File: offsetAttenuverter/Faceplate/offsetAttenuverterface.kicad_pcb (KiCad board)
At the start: 2 copper layers, 20.3 x 128.6 mm, 10 parts

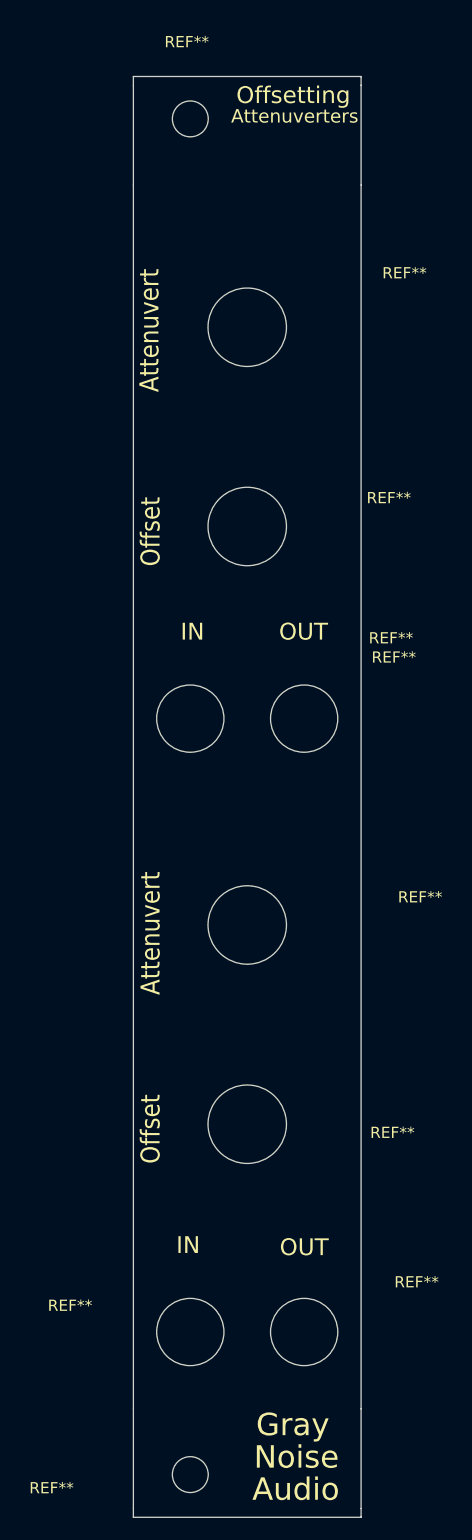
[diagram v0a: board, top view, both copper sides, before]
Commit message: fixing drill holes, adding logo
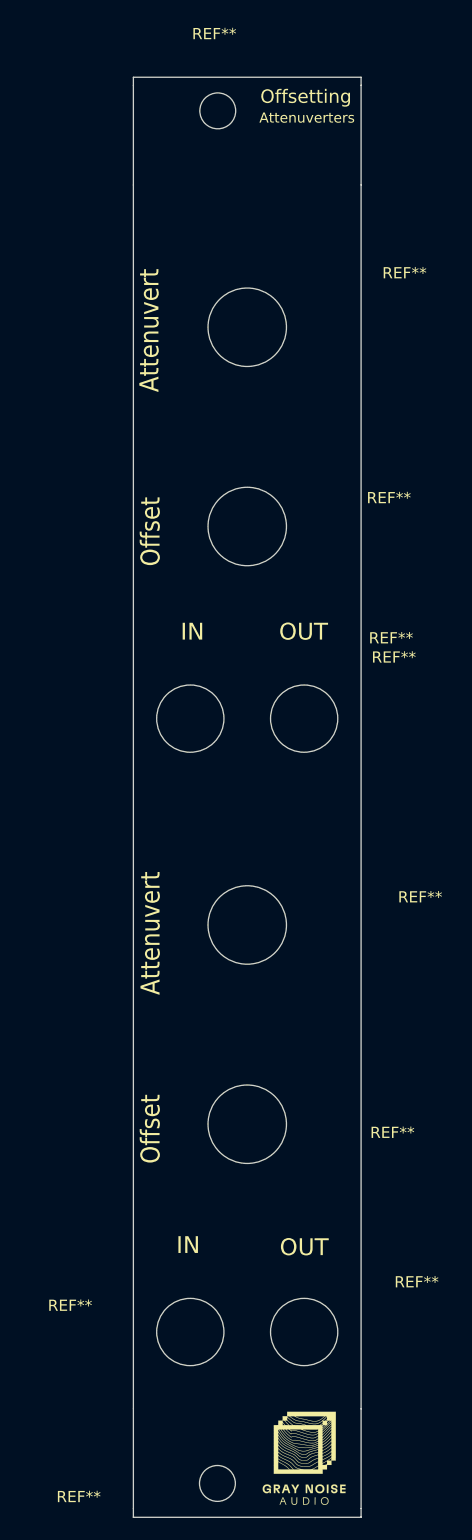
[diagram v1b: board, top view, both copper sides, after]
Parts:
- removed the REF** at (30.5, 158.3)
- removed the REF** at (30.5, 37.3)
- added G***: LOGO, GrayNoise:11mmLogo, F.Cu at (40.7, 156.9)
- added REF**: MountingHole_3.2mm_M3, MountingHole:MountingHole_3.2mm_M3, F.Cu at (32.9, 159.1)
- added REF**: MountingHole_3.2mm_M3, MountingHole:MountingHole_3.2mm_M3, F.Cu at (32.9, 36.6)
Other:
- board size 20.3 x 128.6 mm -> 20.3 x 128.5 mm
- board text removed: "Audio"
- board text removed: "Gray"
- board text removed: "Noise"
